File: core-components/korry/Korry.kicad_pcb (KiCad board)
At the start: 2 copper layers, 104.8 x 105 mm, 176 parts, among them J1 Conn_01x02_Pin, J2 Conn_01x04_Pin

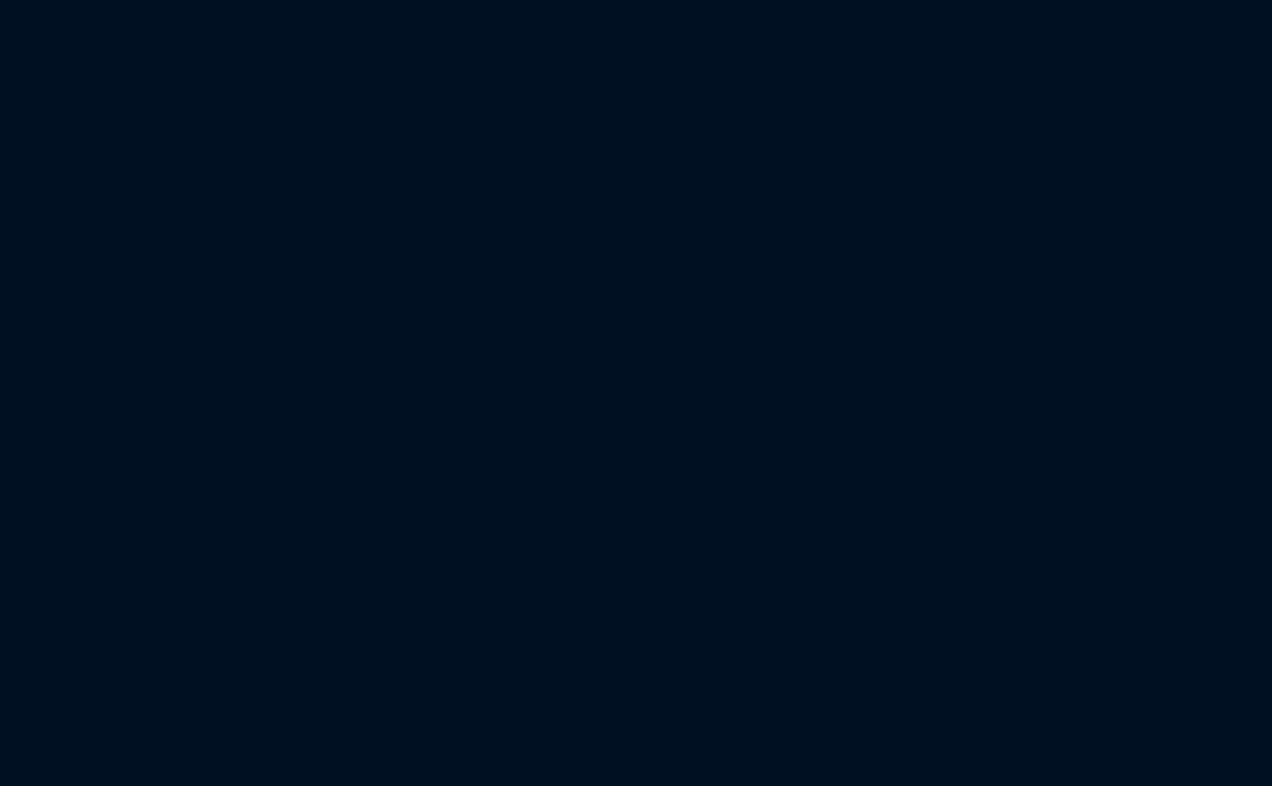
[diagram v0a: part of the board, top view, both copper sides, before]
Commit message: Add 5mm LED footprints and KiCad settings
Add multiple generated LED_THT:LED_D5.0mm footprints to the Korry footprint library (core-components/korry/Korry.kicad_pcb). Update project settings in OpenA3XX.kicad_pro with expanded design defaults, rule severities, DRC rules, teardrop and tuning pattern parameters. Also add Korry library project files (Korry.kicad_pro, Korry.kicad_prl, fp-info-cache) and two OpenA3XX backup ZIPs under OpenA3XX-backups.
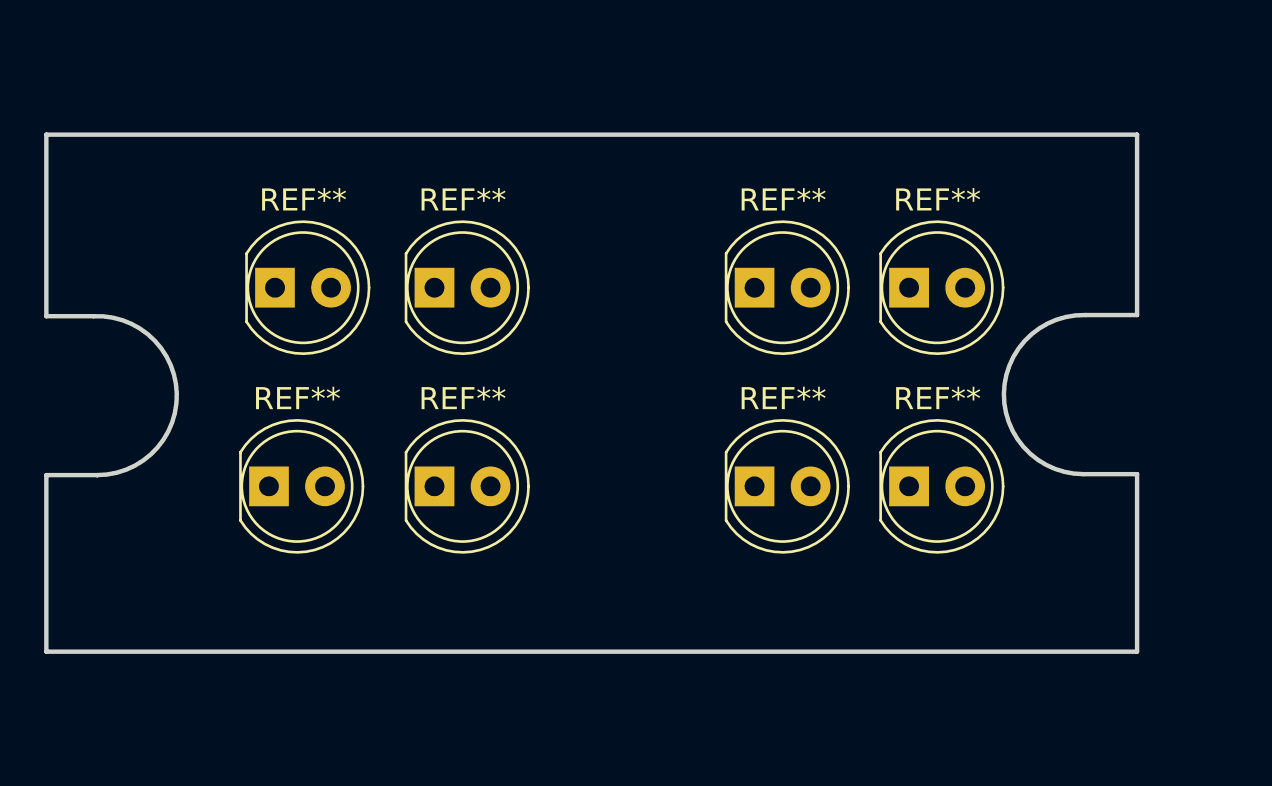
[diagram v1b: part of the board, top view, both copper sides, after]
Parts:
- added REF**: LED_D5.0mm, LED_THT:LED_D5.0mm, F.Cu at (66.3, 99.0)
- added REF**: LED_D5.0mm, LED_THT:LED_D5.0mm, F.Cu at (44.8, 108.0)
- added REF**: LED_D5.0mm, LED_THT:LED_D5.0mm, F.Cu at (66.3, 108.0)
- added REF**: LED_D5.0mm, LED_THT:LED_D5.0mm, F.Cu at (44.8, 99.0)
- added REF**: LED_D5.0mm, LED_THT:LED_D5.0mm, F.Cu at (59.3, 108.0)
- added REF**: LED_D5.0mm, LED_THT:LED_D5.0mm, F.Cu at (37.3, 108.0)
- added REF**: LED_D5.0mm, LED_THT:LED_D5.0mm, F.Cu at (37.6, 99.0)
- added REF**: LED_D5.0mm, LED_THT:LED_D5.0mm, F.Cu at (59.3, 99.0)
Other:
- board size 104.8 x 105 mm -> 173.7 x 105 mm
